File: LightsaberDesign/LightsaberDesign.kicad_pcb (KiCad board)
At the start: 4 copper layers, 77.5 x 20.3 mm, 52 parts, among them J1 Conn_ARM_JTAG_SWD_10, M1 Motor_DC, Q1 Q_PMOS_GSD, Q2 Q_NMOS_GSD, Q3 Q_NMOS_GSD, Q4 Q_NMOS_GSD, SW1 SW_Push, SW2 SW_DIP_x01, SW3 SW_Push, SW4 SW_Push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

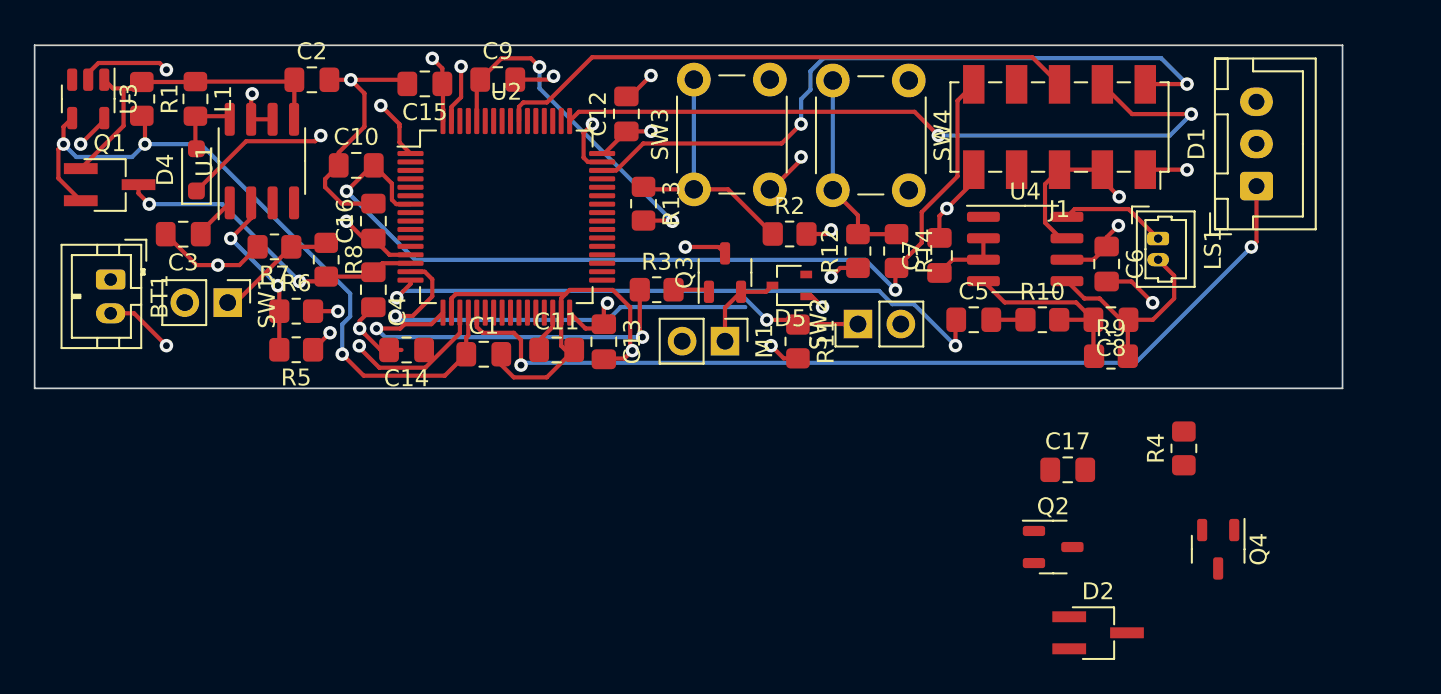
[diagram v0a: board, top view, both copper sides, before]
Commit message: Added crystal, ferrite bead
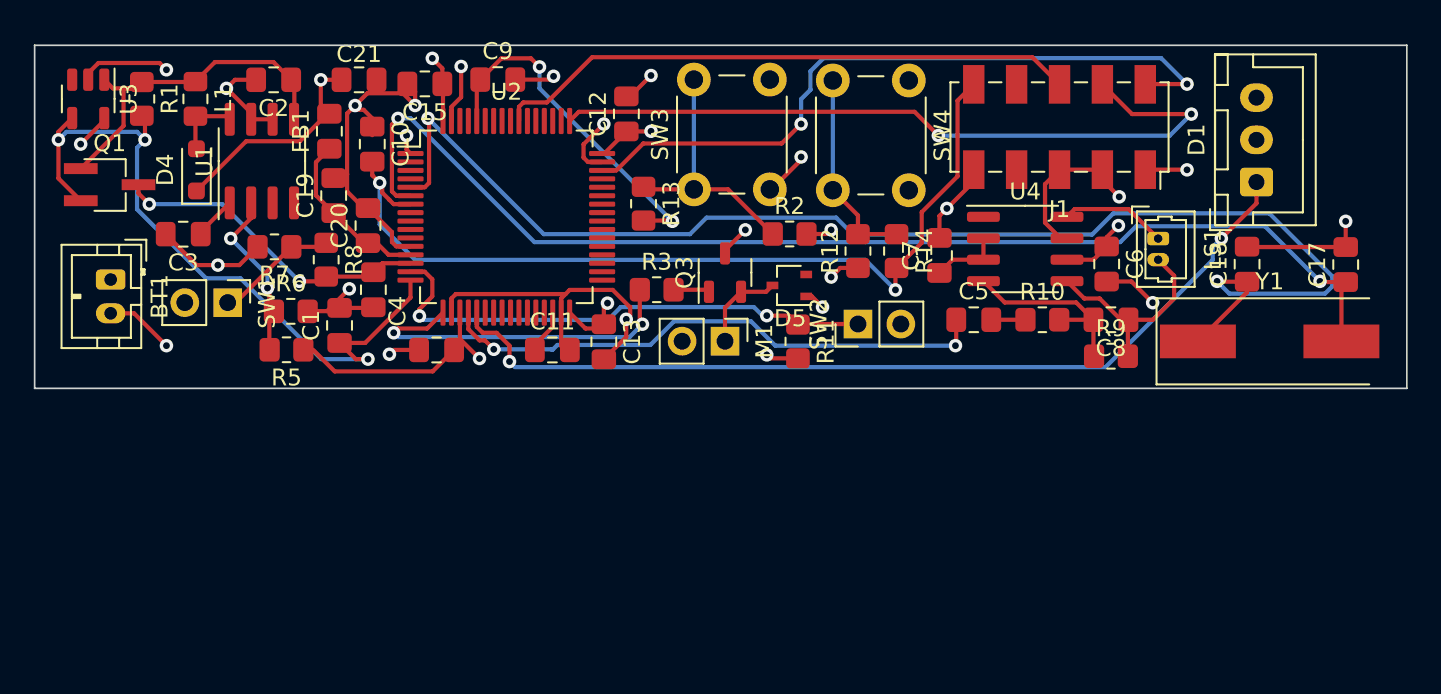
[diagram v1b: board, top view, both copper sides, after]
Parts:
- removed C16: 1uF, Capacitor_SMD:C_0805_2012Metric_Pad1.18x1.45mm_HandSolder
- removed D2: D, Package_TO_SOT_SMD:TSOT-23_HandSoldering
- removed Q2, Q4: Q_NMOS_GSD, Package_TO_SOT_SMD:SOT-23-3
- removed R4: 10k, Resistor_SMD:R_0805_2012Metric_Pad1.20x1.40mm_HandSolder
- added C18: 20pF, Capacitor_SMD:C_0805_2012Metric_Pad1.18x1.45mm_HandSolder, F.Cu at (211.6, 69.6)
- added C19: 1uF, Capacitor_SMD:C_0805_2012Metric_Pad1.18x1.45mm_HandSolder, F.Cu at (157.5, 65.5)
- added C20: 1uF, Capacitor_SMD:C_0805_2012Metric_Pad1.18x1.45mm_HandSolder, F.Cu at (159.5, 67.3)
- added C21: 1uF, Capacitor_SMD:C_0805_2012Metric_Pad1.18x1.45mm_HandSolder, F.Cu at (159.0, 58.7)
- added FB1: FerriteBead, Capacitor_SMD:C_0805_2012Metric_Pad1.18x1.45mm_HandSolder, F.Cu at (157.2, 61.7)
- added Y1: Crystal, Crystal:Crystal_SMD_HC49-SD, F.Cu at (212.9, 74.2)
- C17: value 1uF -> 20pF
- moved C17 20.5 mm to (217.4, 69.6), turned to 90 degrees
- moved C1 8.71 mm to (157.8, 73.2), turned to 90 degrees
- moved C2 2.26 mm to (153.9, 58.7), turned to 180 degrees
- moved C14 1.78 mm to (163.6, 74.7)
- moved C10 1.58 mm to (159.8, 62.5), turned to -90 degrees
- moved R5 0.57 mm to (154.7, 74.7)
- moved R6 0.32 mm to (154.9, 72.4)
- moved C11 0.25 mm to (170.4, 74.7)
- moved D1 0.24 mm to (212.1, 64.7)
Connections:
- C17 pad 1: +3V8 -> Net-(U2-PH1)
- U2 pad 13: +3V8 -> VDDA
- U2 pad 16: /Speaker -> /on_off_switch
- U2 pad 20: /on_off_switch -> /Speaker
- U2 pad 5: unconnected-(U2-PH0-Pad5) -> Net-(U2-PH0)
- U2 pad 6: unconnected-(U2-PH1-Pad6) -> Net-(U2-PH1)
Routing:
- net Net-(U2-PH0): track 0.00 -> 78.8 mm, vias 0 -> 2
- net Net-(U2-PH1): track 0.00 -> 70.2 mm, vias 0 -> 2
- net VDDA: track 0.00 -> 10.5 mm
- net GND: track 101.3 -> 109.9 mm, vias 18 -> 20
- net /Speaker: track 37.5 -> 33.2 mm
- net /Shake: track 33.6 -> 30.8 mm
- net /NRST: track 54.7 -> 52.0 mm
- net /Motor: track 23.2 -> 20.7 mm
- net /LED: track 55.2 -> 54.0 mm
- net Net-(U1-FB): track 10.4 -> 9.56 mm
- net +3V0: track 20.5 -> 21.4 mm
- net +3V8: track 51.5 -> 50.7 mm, vias 13 -> 11
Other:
- board size 77.5 x 20.3 mm -> 81.3 x 20.3 mm

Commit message: Finished drc
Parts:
- added REF**: Phoenix_Graphic, Graphics:Phoenix_Graphic, F.Cu at (218.2, 59.9)
- M1: footprint Connector_PinHeader_2.54mm:PinHeader_1x02_P2.54mm_Vertical -> Connector_Molex:Molex_PicoBlade_53047-0210_1x02_P1.25mm_Vertical
- SW2: footprint Connector_PinHeader_2.54mm:PinHeader_1x02_P2.54mm_Vertical -> Capacitor_THT:CP_Radial_D4.0mm_P1.50mm
- moved SW2 0.86 mm to (189.0, 73.9)
- moved M1 0.28 mm to (180.6, 74.4), turned to 180 degrees
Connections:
- D1 pad 2: +5V -> +3V8
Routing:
- net /Shake: track 30.8 -> 31.5 mm
- net /Speaker: track 33.2 -> 33.8 mm

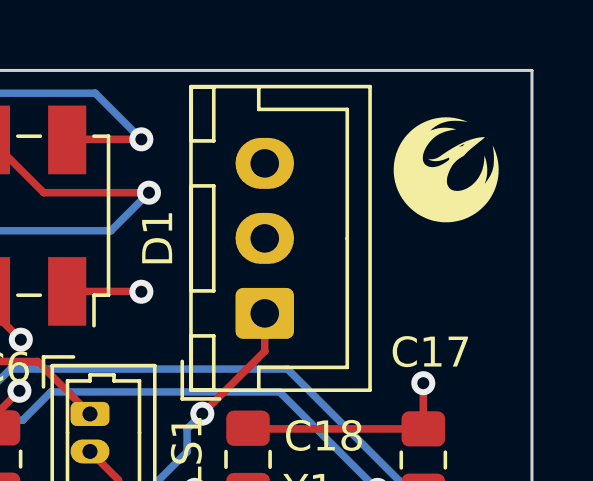
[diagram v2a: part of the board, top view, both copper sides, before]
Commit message: Updated capacitor values
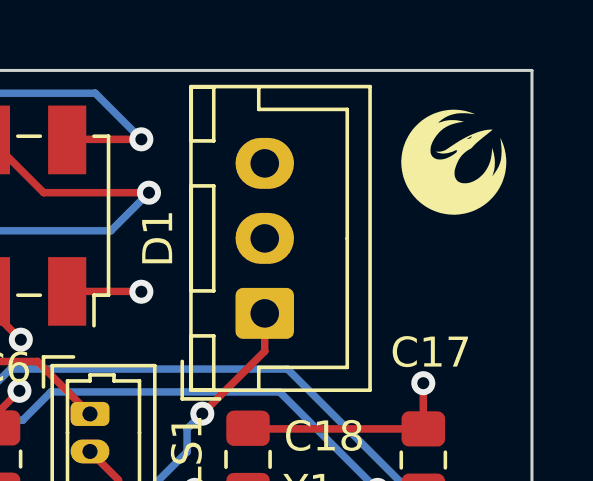
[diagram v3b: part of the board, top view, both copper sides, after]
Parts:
- C12, C13, C14, C15: value 1uF -> .1uF
- C19: value 1uF -> 10nF
- C4: value 1u -> 1uF
- moved REF** 0.36 mm to (218.4, 59.7)

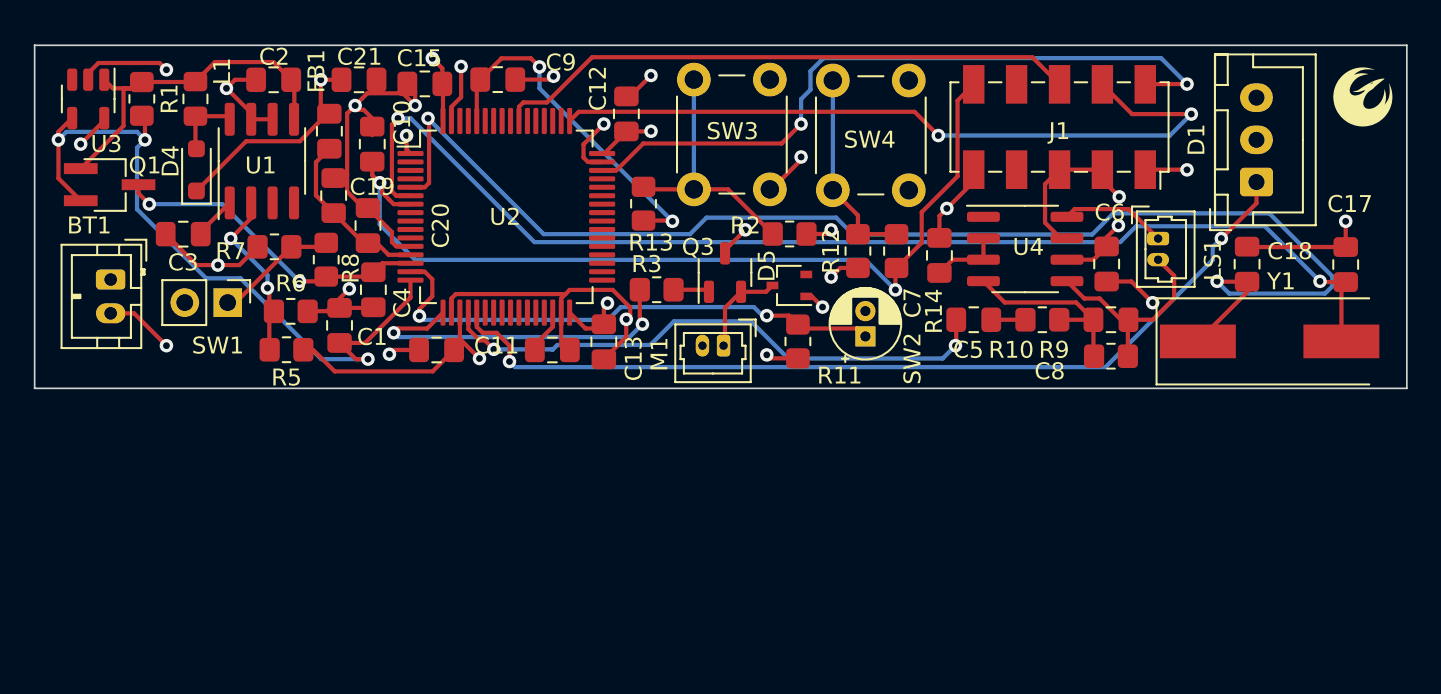
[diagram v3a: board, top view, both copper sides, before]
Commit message: Updated PCB with new header
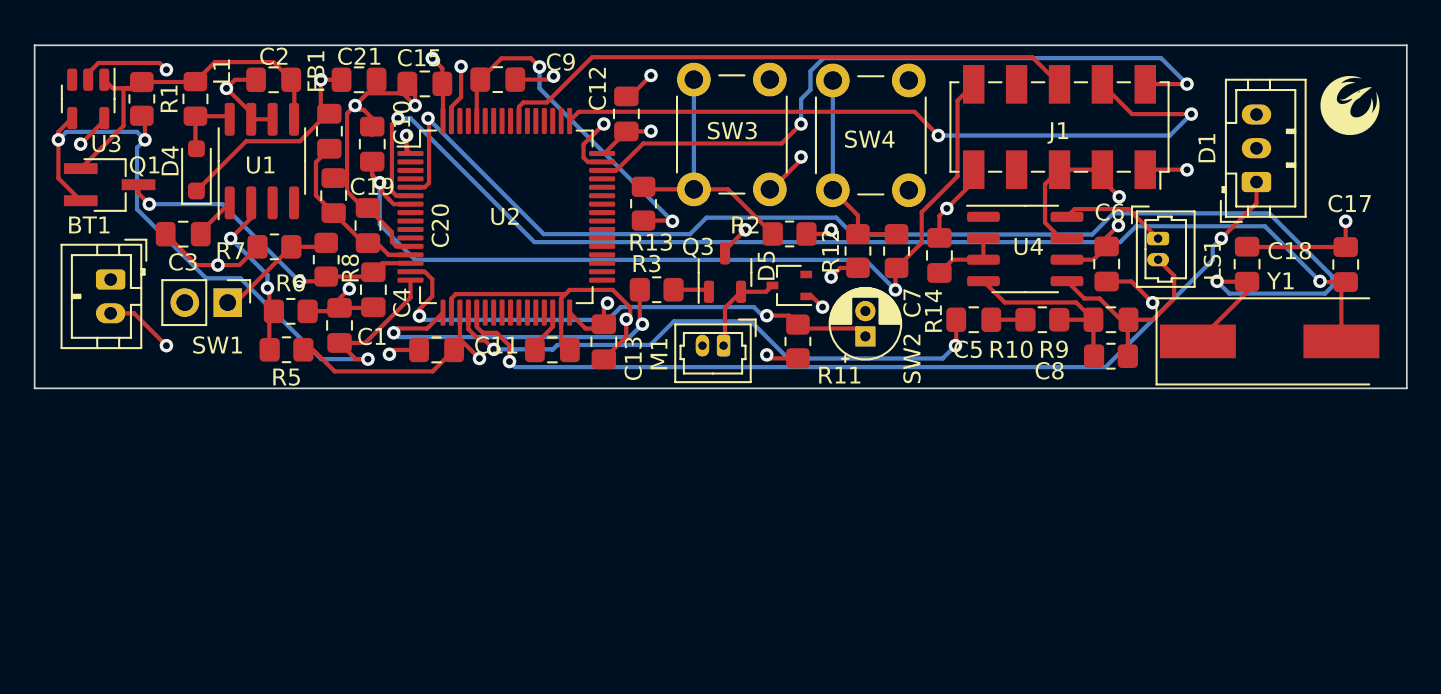
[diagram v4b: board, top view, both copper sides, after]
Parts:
- D1: footprint Connector_JST:JST_XH_B3B-XH-A_1x03_P2.50mm_Vertical -> Connector_JST:JST_PH_B3B-PH-K_1x03_P2.00mm_Vertical
- moved REF** 0.92 mm to (217.7, 60.2)
